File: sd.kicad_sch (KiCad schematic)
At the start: 81 parts, among them J2 MicroSD_1140084168, J4 USB-C_GCT_USB4105-GF-A, J5 USB-A_UJ2-AH-4-SMT-TR, Q1 PJE138K, Q2 PJE138K, U1 USB2642_ML, U2 AP22615A_TSOT26, U3 AP22615A_TSOT26, U5 FUSB303B, Y2 Resonator_24MHz_ABM8G

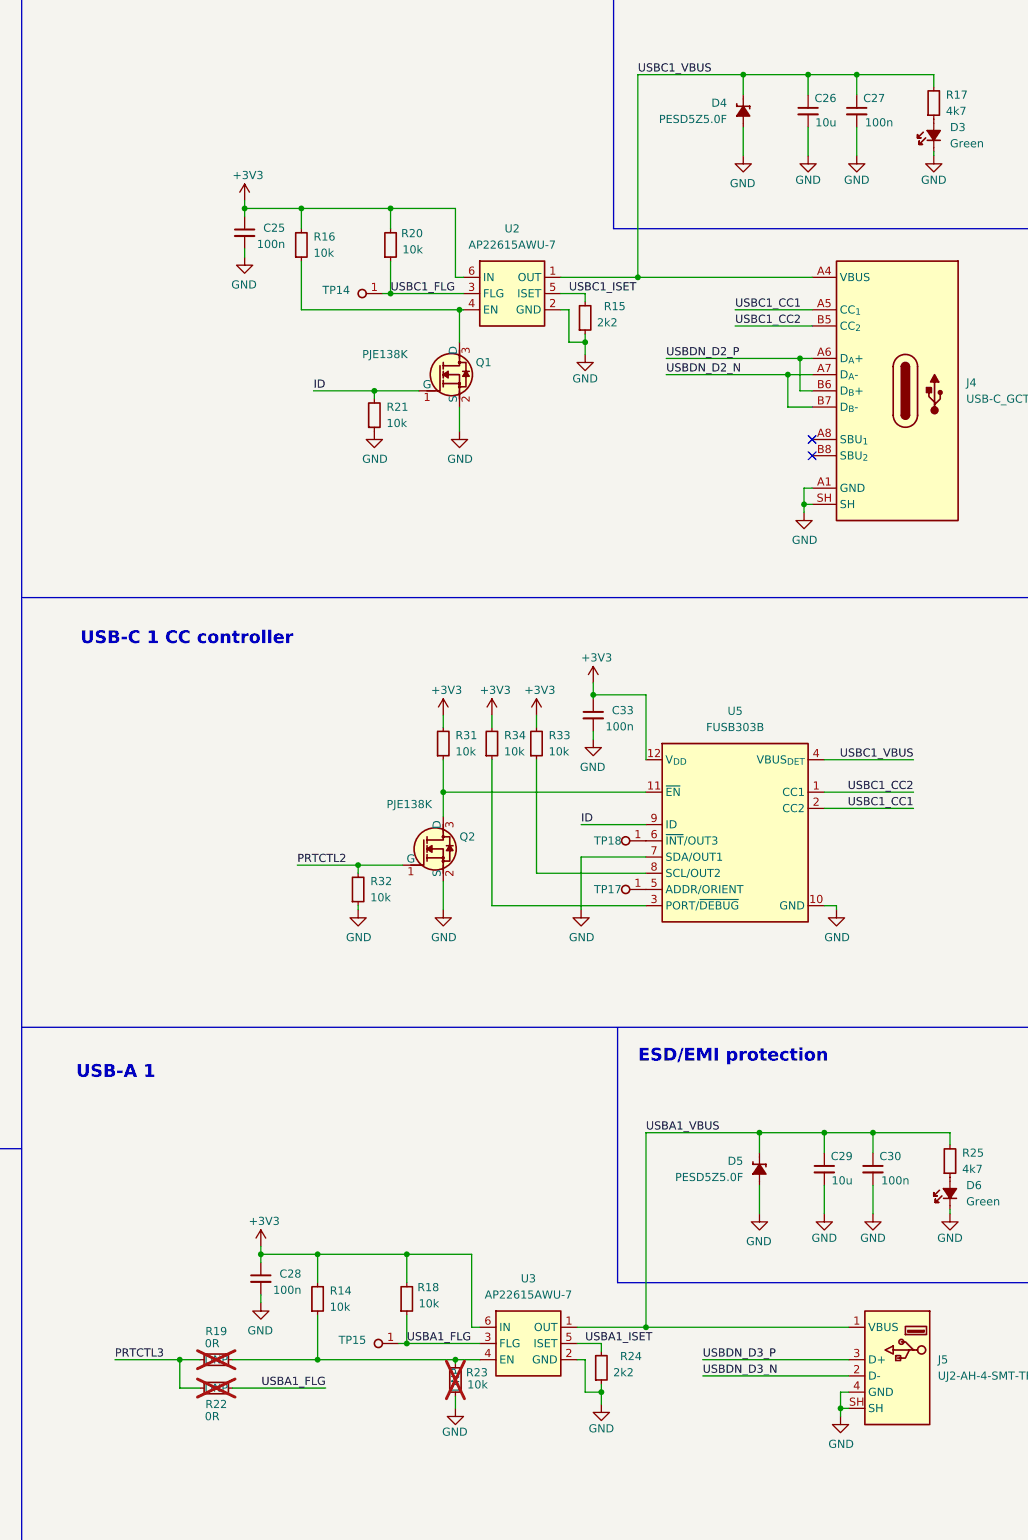
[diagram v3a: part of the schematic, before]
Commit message: [#64333] Fixed schematic after review
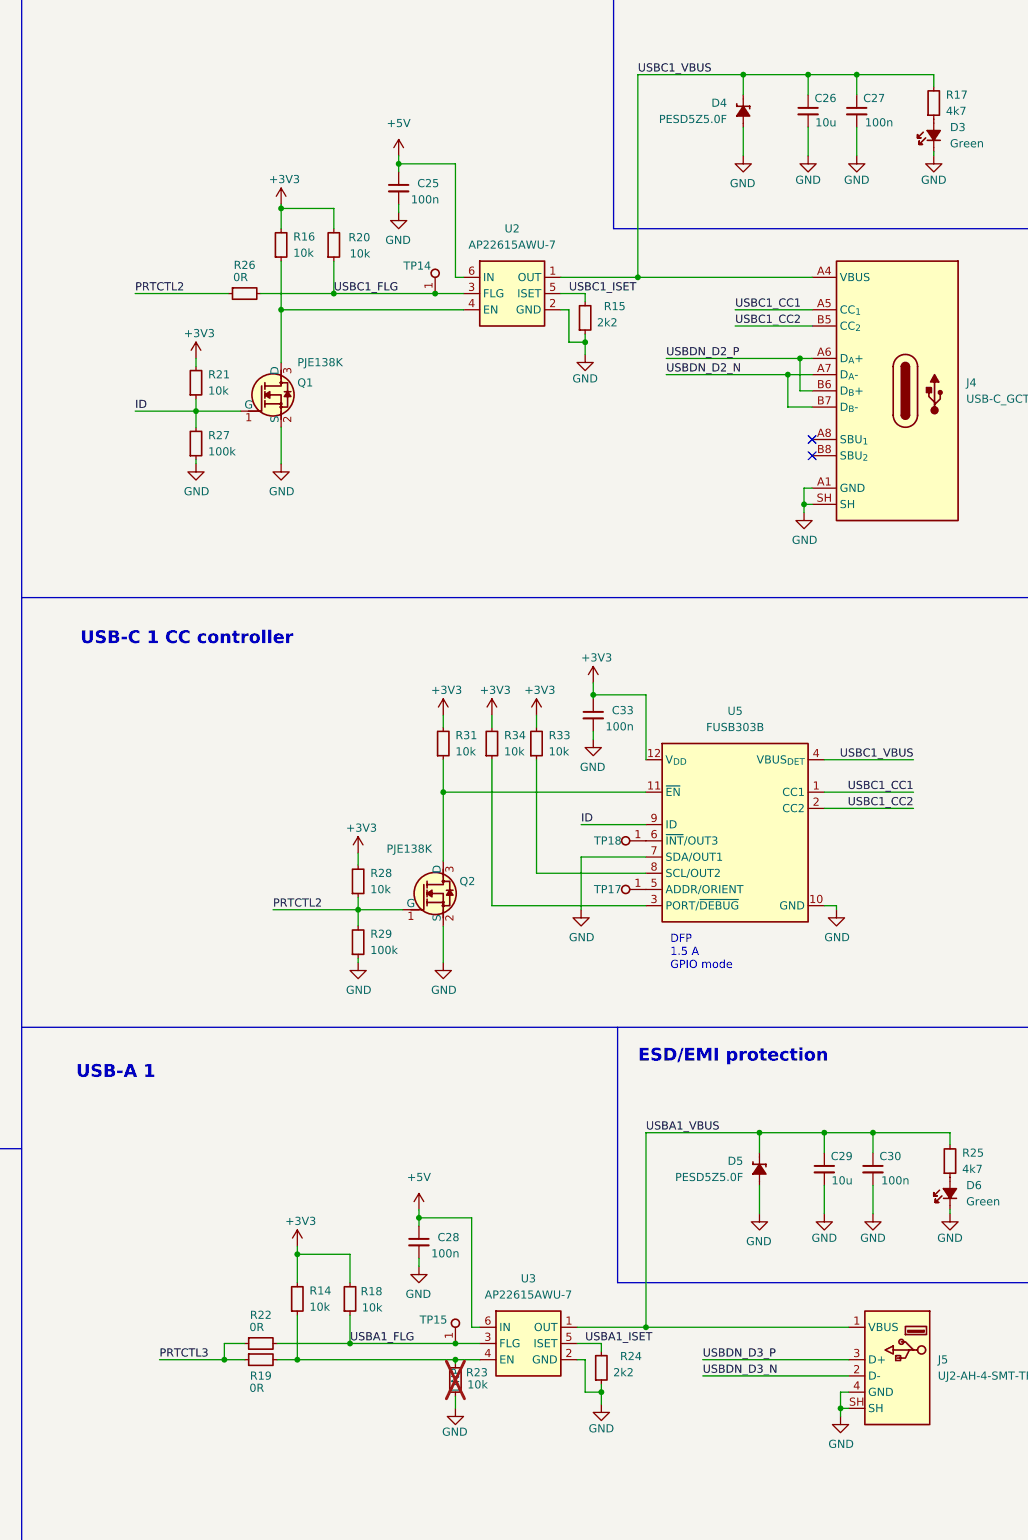
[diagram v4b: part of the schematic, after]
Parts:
- removed R32: R_10k_0402, antmicro-footprints:R_0402_1005Metric, symbol antmicroResistors0402:R_10k_0402
- added R26: R_0R_0402, antmicro-footprints:R_0402_1005Metric, symbol antmicroResistors0402:R_0R_0402
- added R27, R29: R_100k_0402, antmicro-footprints:R_0402_1005Metric, symbol antmicroResistors0402:R_100k_0402
- added R28: R_10k_0402, antmicro-footprints:R_0402_1005Metric, symbol antmicroResistors0402:R_10k_0402
- R19, R22: now fitted; now in the parts list
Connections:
- net +3V3: now also R21.2, R28.2; no longer C25.1, C28.1, U2.6 (IN), U3.6 (IN)
- net GND: now also R27.1, R29.1; no longer R21.1
- net ID: now also R21.1, R27.2; no longer R21.2
- net PRTCTL2: now also R26.1, R28.1, R29.2
- net USBC1_CC1: now also U5.1 (CC1); no longer U5.2 (CC2)
- net USBC1_CC2: now also U5.2 (CC2); no longer U5.1 (CC1)
- net USBC1_FLG: now also R26.2
- new net +5V: C25.1, C28.1, U2.6 (IN), U3.6 (IN)
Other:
- note added: "DFP 1.5 A GPIO mode"
- moved on the sheet: C25, Q1, Q2, R14, R16, R18, R20, R21, TP14, TP15

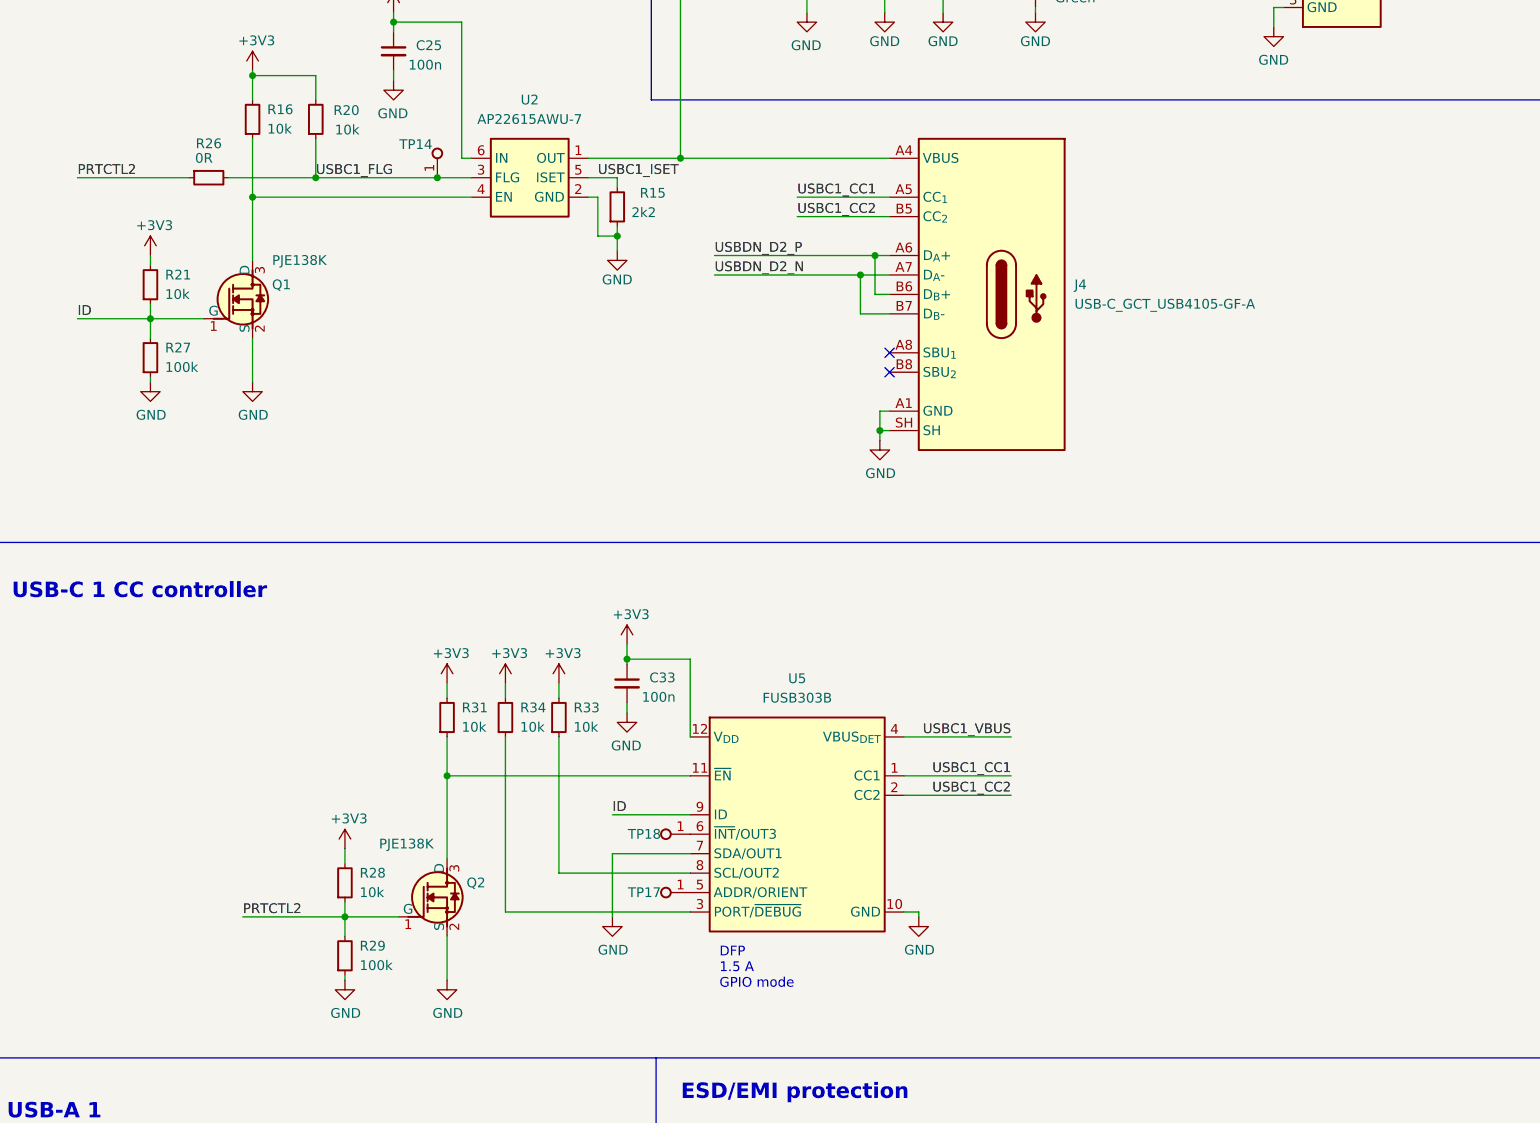
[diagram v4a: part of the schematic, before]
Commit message: [#64333] Added usb to net class and added via stitching
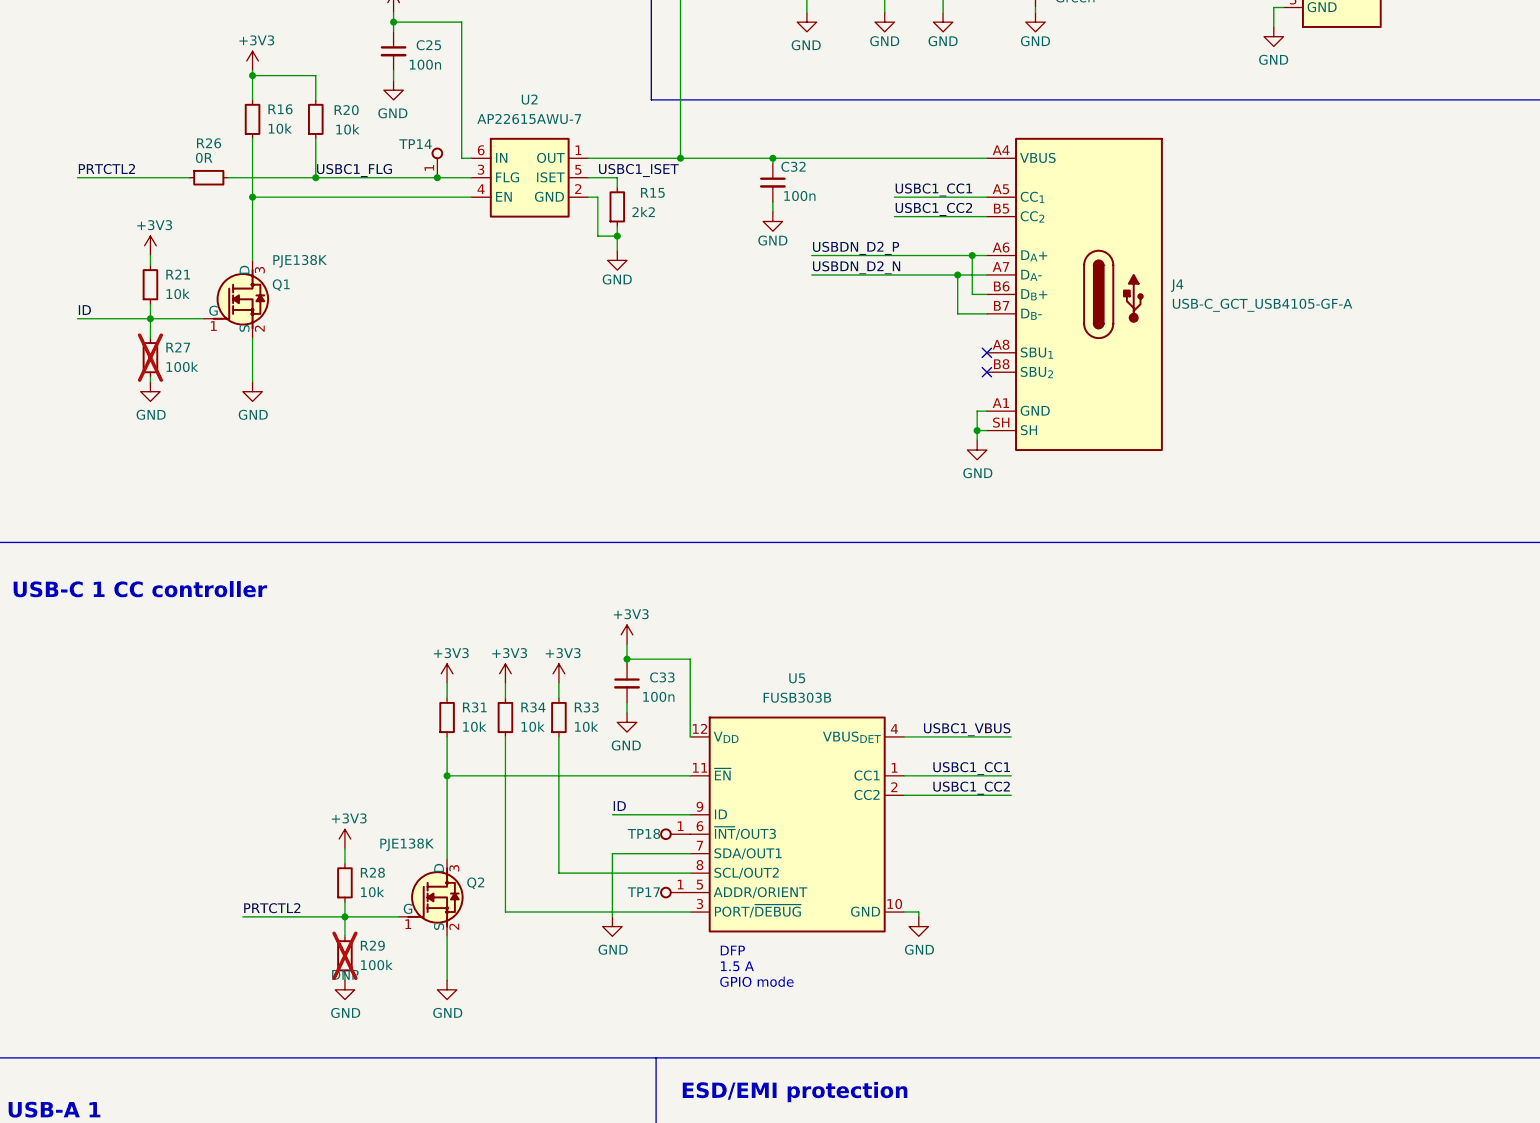
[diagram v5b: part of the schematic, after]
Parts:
- added C32: C_100n_0402, antmicro-footprints:C_0402_1005Metric, symbol antmicroCapacitors0402:C_100n_0402
- R27, R29: DNP (none) -> DNP; now not fitted; now left out of the parts list
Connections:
- net GND: now also C32.2
- net USBC1_VBUS: now also C32.1
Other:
- moved on the sheet: J4

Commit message: Updated symbols from lib. Minor DRC and ERC fixes
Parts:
- C26, C29: Dielectric (none) -> template_dielectric
- D2: Color (none) -> Green
- U2, U3: MPN AP22615AWU-7 -> AP22615AWU-7
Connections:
- net GND: now also D2.1 (C); no longer D2.2
- net at R6.1: now also D2.2 (A); no longer D2.1
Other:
- moved on the sheet: C21, C22, C25, C28, C29, C30, C32, C33, D2, D3, D5, D6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

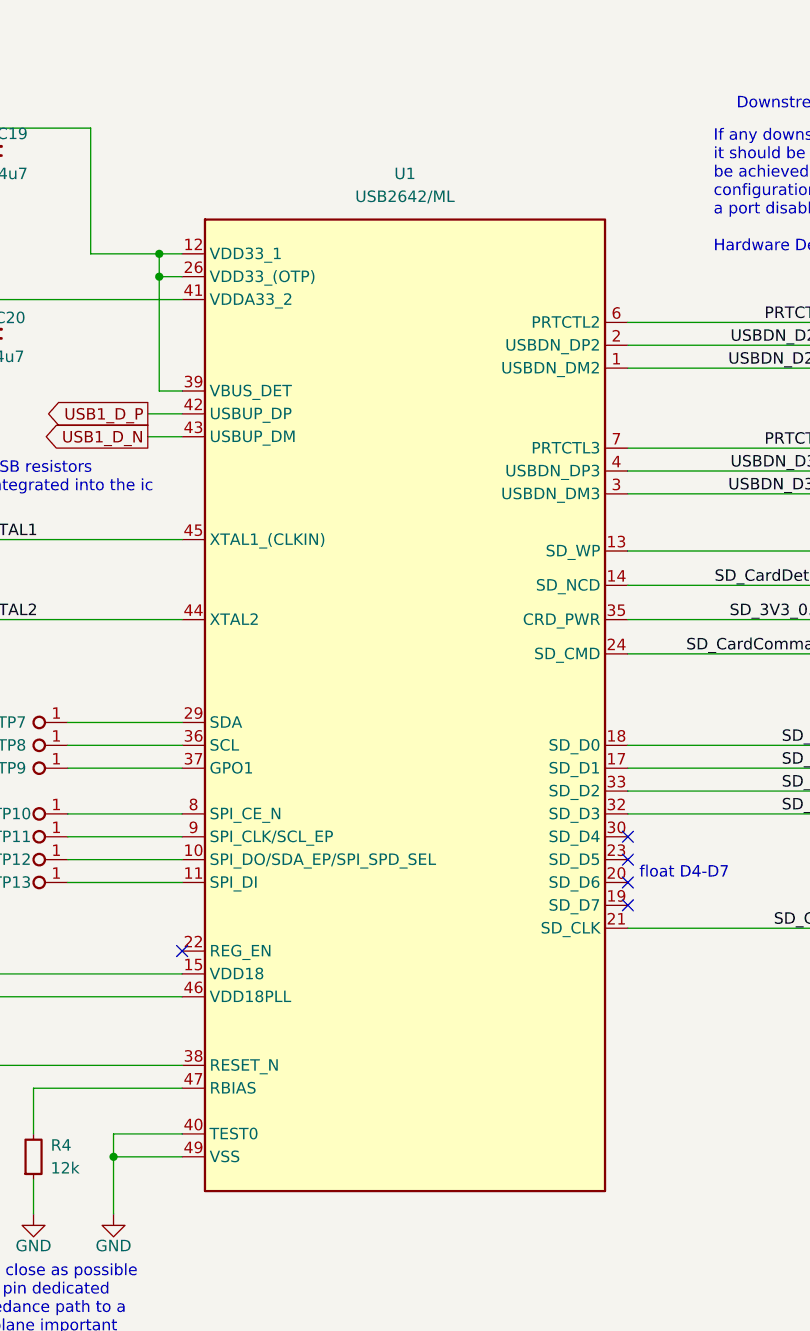
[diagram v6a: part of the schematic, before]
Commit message: [#67311] Replace symbol and footprint of U1, Bump revision
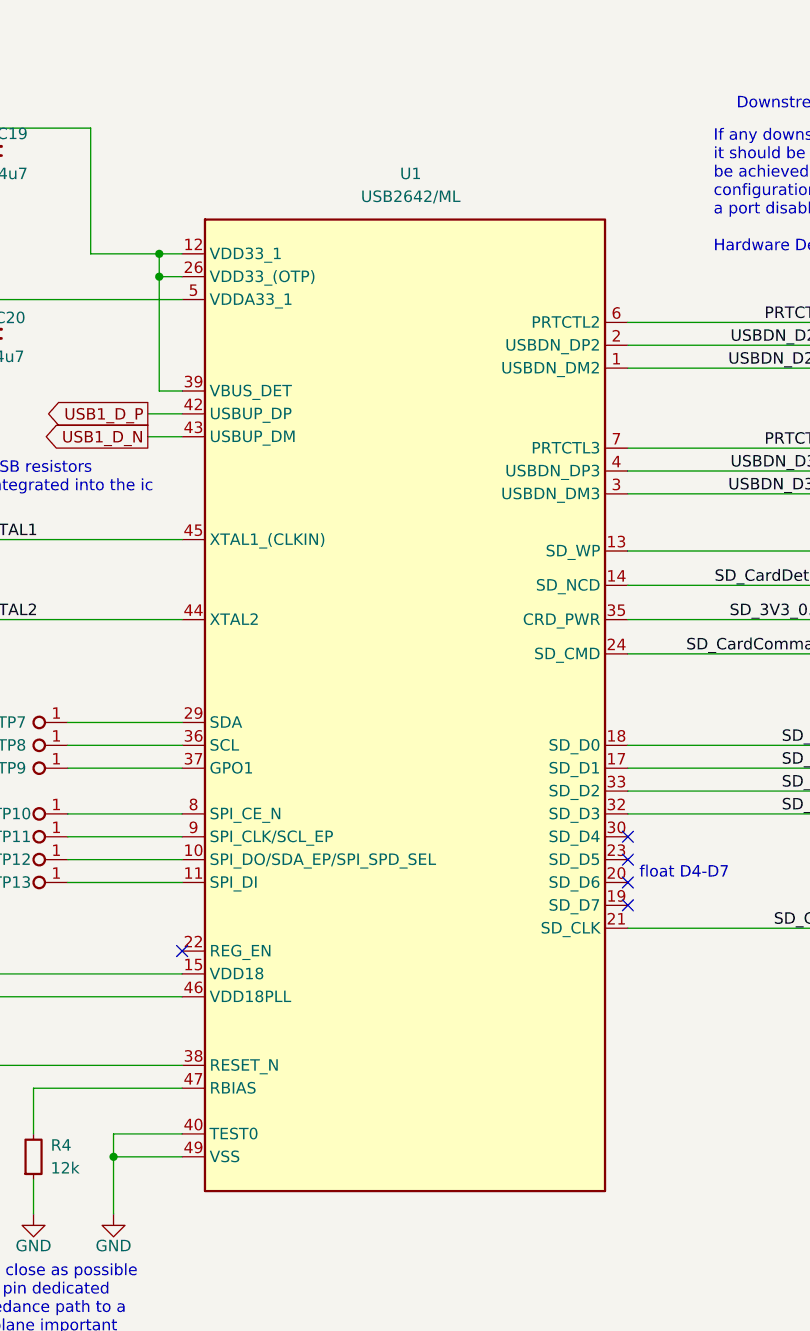
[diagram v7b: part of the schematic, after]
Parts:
- U1: footprint antmicro-footprints:QFN-48-Microchip-QFN77-48LD-PL-2 -> antmicro-footprints:QFN-48-1EP_7x7x0.9mm_P0.5mm_EP5x5mm
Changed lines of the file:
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@@
   (title_block
     (title "Jetson Orin Baseboard Storage Expansion")
-    (date "2024-08-20")
-    (rev "1.2.0")
+    (date "2024-10-15")
+    (rev "1.2.1")
     (company "Antmicro Ltd")
   )
@@
     )
   )
-  (symbol (lib_id "antmicroInterfaceControllers:USB2642_ML") (at 130.81 64.77 0) (unit 1)
-    (in_bom yes) (on_board yes) (dnp no) (fields_autoplaced)
-    (property "Reference" "U1" (at 106.045 43.18 0)
+  (symbol (lib_id "antmicroInterfaceControllers:USB2642_ML") (at 81.28 52.07 0) (unit 1)
+    (in_bom yes) (on_board yes) (dnp no)
+    (property "Reference" "U1" (at 106.68 43.18 0)
       (effects (font (size 1.27 1.27) (thickness 0.15)))
     )
-    (property "Value" "USB2642_ML" (at 157.48 59.69 0)
+    (property "Value" "USB2642_ML" (at 107.95 46.99 0)
       (effects (font (size 1.27 1.27) (thickness 0.15)) (justify left bottom) hide)
     )
-    (property "Footprint" "antmicro-footprints:QFN-48-Microchip-QFN77-48LD-PL-2" (at 157.48 62.23 0)
+    (property "Footprint" "antmicro-footprints:QFN-48-1EP_7x7x0.9mm_P0.5mm_EP5x5mm" (at 107.95 49.53 0)
       (effects (font (size 1.27 1.27) (thickness 0.15)) (justify left bottom) hide)
     )
-    (property "Datasheet" "https://ww1.microchip.com/downloads/en/DeviceDoc/00001578D.pdf" (at 157.48 64.77 0)
+    (property "Datasheet" "https://ww1.microchip.com/downloads/en/DeviceDoc/00001578D.pdf" (at 107.95 52.07 0)
       (effects (font (size 1.27 1.27) (thickness 0.15)) (justify left bottom) hide)
     )
-    (property "MPN" "USB2642/ML" (at 106.045 45.72 0)
+    (property "MPN" "USB2642/ML" (at 106.68 45.72 0)
       (effects (font (size 1.27 1.27) (thickness 0.15)))
     )
-    (property "Manufacturer" "Microchip Technology" (at 157.48 69.85 0)
+    (property "Manufacturer" "Microchip Technology" (at 107.95 57.15 0)
       (effects (font (size 1.27 1.27) (thickness 0.15)) (justify left bottom) hide)
     )
-    (property "Description" "USB 2.0 Hub and Flash Media Card Controller Combo" (at 157.48 72.39 0)
+    (property "Description" "USB 2.0 Hub and Flash Media Card Controller Combo" (at 107.95 59.69 0)
       (effects (font (size 1.27 1.27) (thickness 0.15)) (justify left bottom) hide)
     )
-    (property "License" "Apache-2.0" (at 157.48 74.93 0)
+    (property "License" "Apache-2.0" (at 107.95 62.23 0)
       (effects (font (size 1.27 1.27) (thickness 0.15)) (justify left bottom) hide)
     )
-    (property "Author" "Antmicro" (at 157.48 77.47 0)
+    (property "Author" "Antmicro" (at 107.95 64.77 0)
       (effects (font (size 1.27 1.27) (thickness 0.15)) (justify left bottom) hide)
     )
